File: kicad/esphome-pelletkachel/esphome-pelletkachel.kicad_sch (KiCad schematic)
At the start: 16 parts, among them J1 Display-MCU-Connector, J2 Display-MCU-Connector, J3 MOSI-RSTSKIMIS, J4 Thumbs, U1 ESP32-DEVKITC-32U, U2 757, U3 VL53L0CXV0DH1

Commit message: first pcb tests
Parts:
- J4: now left out of the parts list
- JB1, JB2: footprint (none) -> Connector_PinHeader_2.54mm:PinHeader_1x08_P2.54mm_Vertical
- JB3: footprint (none) -> TerminalBlock:TerminalBlock_bornier-2_P5.08mm
- JB4, JB5: footprint (none) -> Connector_JST:JST_XH_S4B-XH-A_1x04_P2.50mm_Horizontal
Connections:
- net +5V: now also JB4.4 (V), JB5.4 (V); no longer JB4.V (Pin_4), JB5.V (Pin_4)
- net GND: now also JB4.3 (G), JB5.3 (G); no longer JB4.G (Pin_3), JB5.G (Pin_3)
- net RX - TuyaMCU renamed RX - Tuya MCU
- net TX - TuyaMCU renamed TX - Tuya MCU
- new net: JB4.1 (T), JB5.1 (T), U2.HV1
- new net: JB4.2 (R), JB5.2 (R), U2.HV2
- no-connect marks 0 -> 87

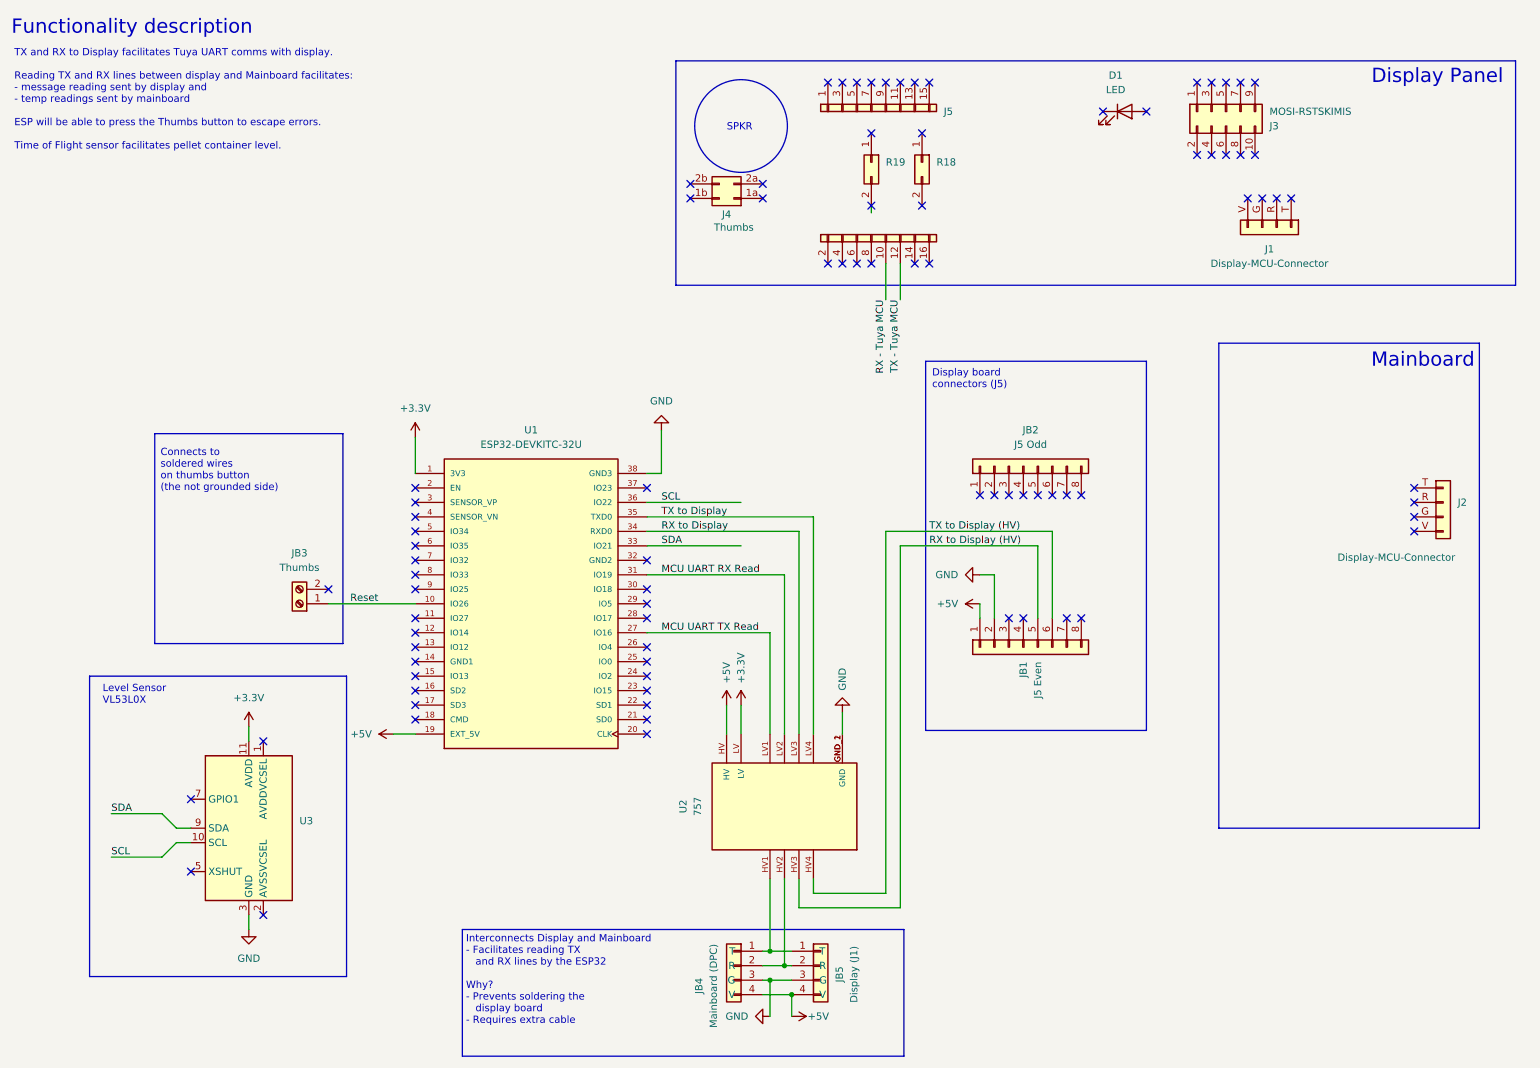
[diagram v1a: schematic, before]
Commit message: changed schematic
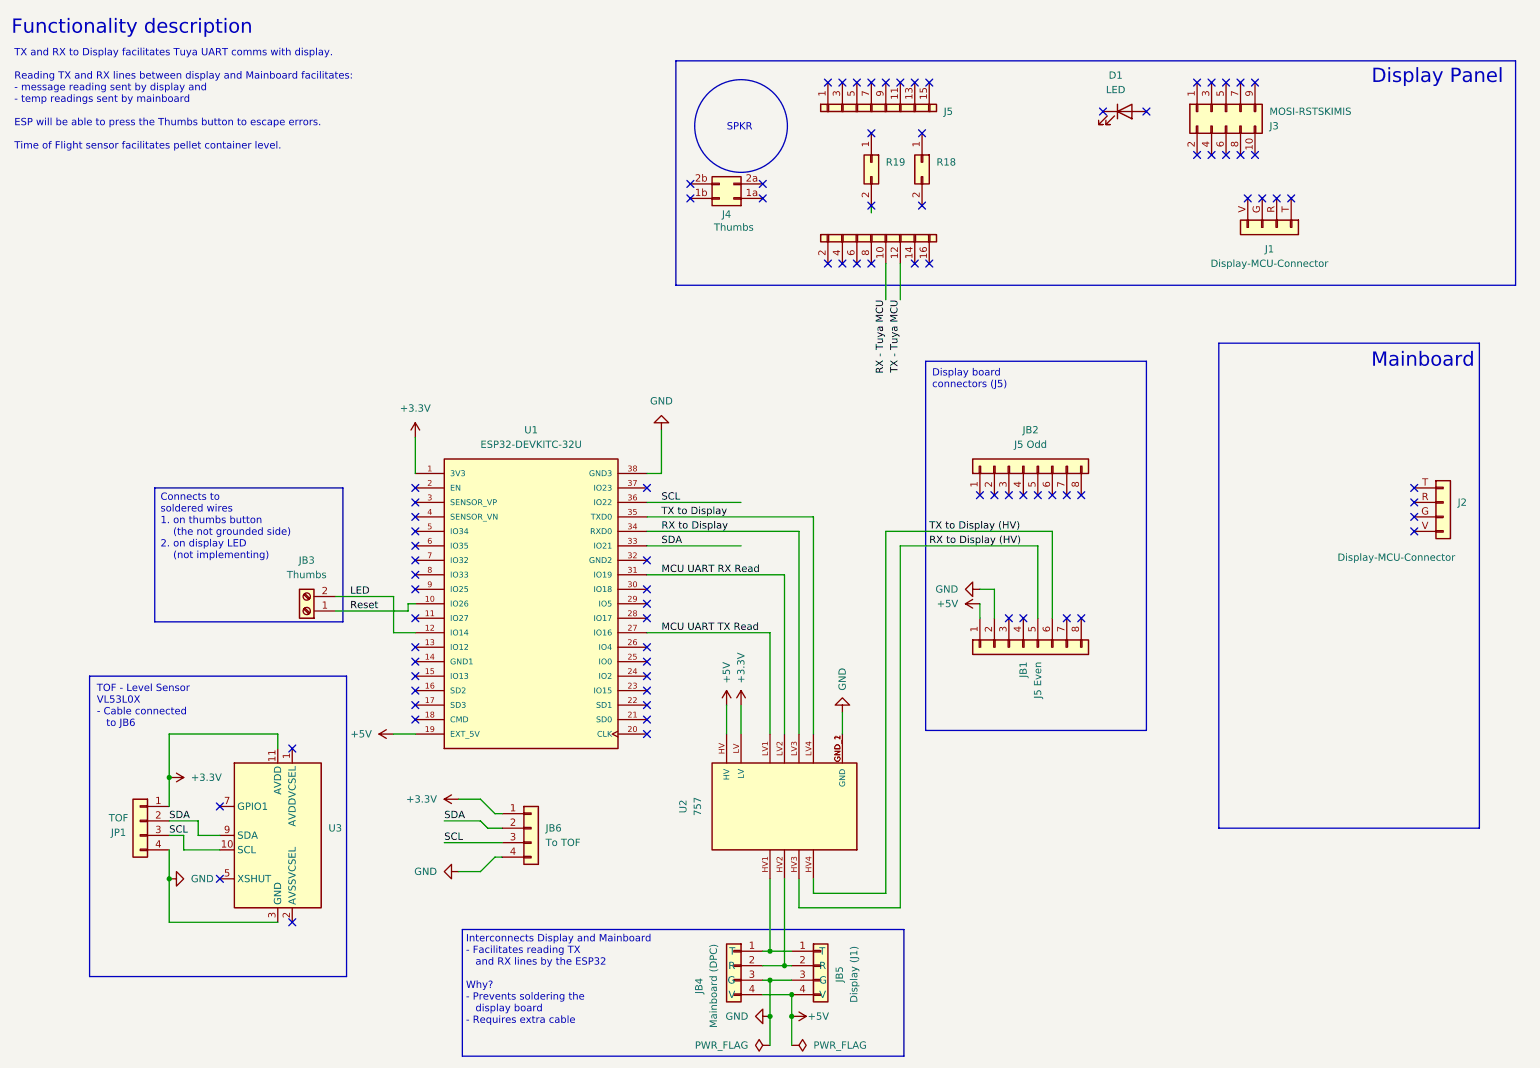
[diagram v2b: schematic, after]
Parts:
- added JB6: To TOF, Connector_JST:JST_XH_S4B-XH-A_1x04_P2.50mm_Horizontal, symbol Connector_Generic:Conn_01x04
- added JP1: TOF, symbol Connector_Generic:Conn_01x04
- U3: now left out of the parts list
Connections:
- net +3.3V: now also JB6.1 (Pin_1), JP1.1 (Pin_1)
- net GND: now also JB6.4 (Pin_4), JP1.4 (Pin_4)
- net SCL: now also JB6.3 (Pin_3), JP1.3 (Pin_3)
- net SDA: now also JB6.2 (Pin_2), JP1.2 (Pin_2)
- net LED: now reaches U1.12 (IO14)
- net LED: now also JB3.2 (Pin_2)
- no-connect marks 87 -> 85
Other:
- note added: "Connects to soldered wires 1. on thumbs button (the not grounded side) 2. on display LED (not implementing)"
- note added: "TOF - Level Sensor VL53L0X - Cable connected to JB6"
- note removed: "Connects to soldered wires on thumbs button (the not grounded side)"
- note removed: "Level Sensor VL53L0X"
- moved on the sheet: JB3, U3

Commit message: annotations
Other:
- note added: "Connector to TOF"
- note added: "LLC"
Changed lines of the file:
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@@
+	)
+	(rectangle
+		(start 82.55 144.78)
+		(end 125.095 167.005)
+		(stroke
+			(width 0)
+			(type default)
+		)
+		(fill
+			(type none)
+		)
 	)
 	(rectangle
@@
 			(type default)
 			(color 0 132 0 1)
+		)
+		(fill
+			(type none)
+		)
+	)
+	(rectangle
+		(start 130.81 123.825)
+		(end 167.005 165.735)
+		(stroke
+			(width 0)
+			(type default)
 		)
 		(fill
@@
 		)
 	)
+	(text "LLC"
+		(exclude_from_sim no)
+		(at 164.338 125.73 0)
+		(effects
+			(font
+				(size 1.27 1.27)
+			)
+		)
+	)
 	(text "Interconnects Display and Mainboard\n- Facilitates reading TX \n   and RX lines by the ESP32\n\nWhy?\n- Prevents soldering the \n   display board\n- Requires extra cable"
 		(exclude_from_sim no)
@@
 		)
 	)
+	(text "Connector to TOF"
+		(exclude_from_sim no)
+		(at 92.202 146.812 0)
+		(effects
+			(font
+				(size 1.27 1.27)
+			)
+		)
+	)
